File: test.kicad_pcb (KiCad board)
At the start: 2 copper layers, 110 x 100 mm, 203 parts, among them J1 HSP2_MX-502584-0670, J2 HSP2_MX-502584-0670, J3 HSP2_MX-502584-0670, J4 HSP2_MX-502584-0670, J5 HSP2_MX-502584-0670, J6 HSP2_MX-502584-0670, J7 CONN_02X01, J8 CONN_02X01, J9 microSD, P1 Gniazdo akumulatora, P2 Gniazdo akumulatora, P3 Gniazdo programatora SWD, T1 IRLML6401, T10 BSS138, T11 BSS138, T12 BSS138, T13 BSS138, T14 FDV304P, T2 IRLML6401, T3 IRLML6401, T4 IRLML6401, T5 IRLML6401, T6 IRLML6401, T7 BSS138, T8 BSS138, T9 BSS138, U1 MCP1755T-3302E/DC, U10 TPS3823, U11 STM32L051R8, U12 DS3231SN, U13 MCP1755T-3302E/DC, U14 MCP1755T-3302E/DC, U15 MIC29302, U16 DHT22, U17 M590E, U18 S25FL1275ABMGI101, U19 ESP-07, U2 MCP1755T-3302E/DC, U20 SIMHOLDER, U3 MCP1755T-3302E/DC, U4 MCP1755T-3302E/DC, U5 MCP1755T-3302E/DC, U6 MCP1755T-3302E/DC, U7 74LVX373M, U8 74LVX373M, U9 MAX3485, Y1 32.768 kHz, Y2 8 MHz

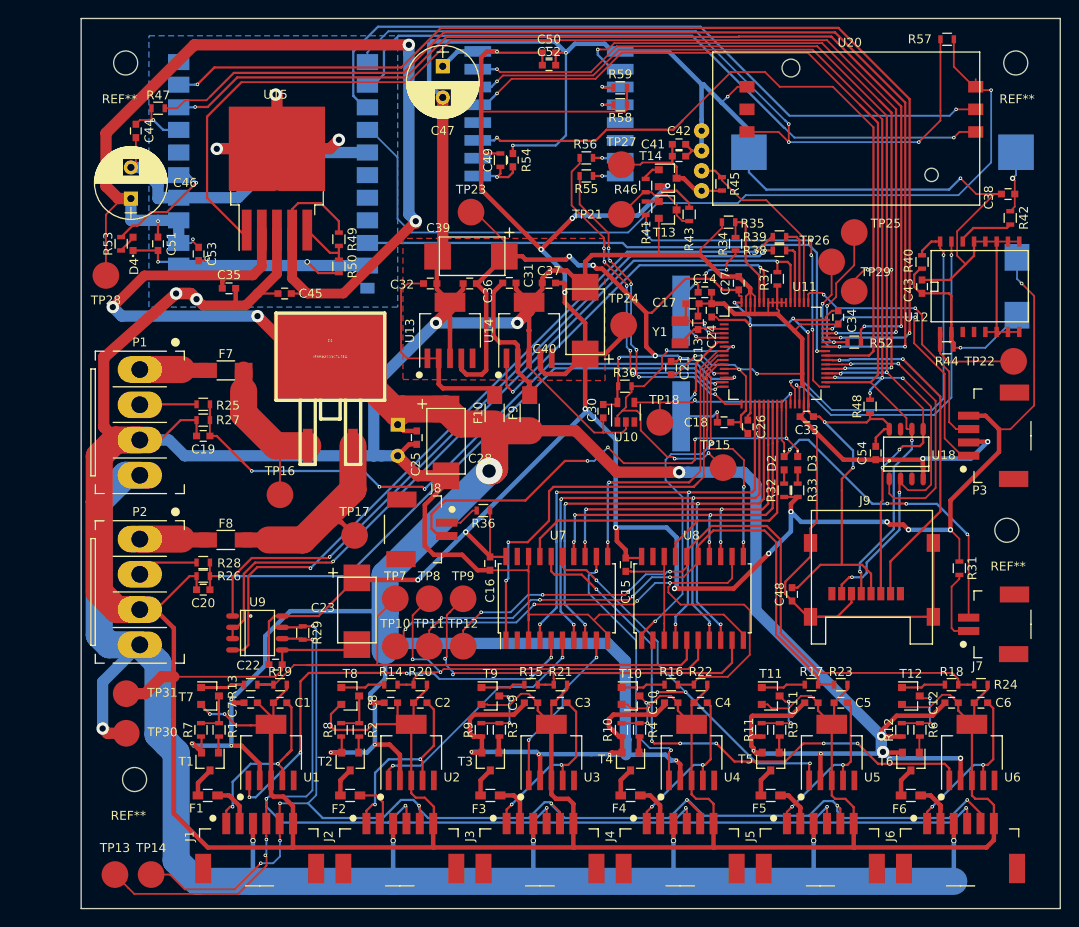
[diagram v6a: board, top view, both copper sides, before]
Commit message: +creo-weipu +zmiana dht22 i c1000
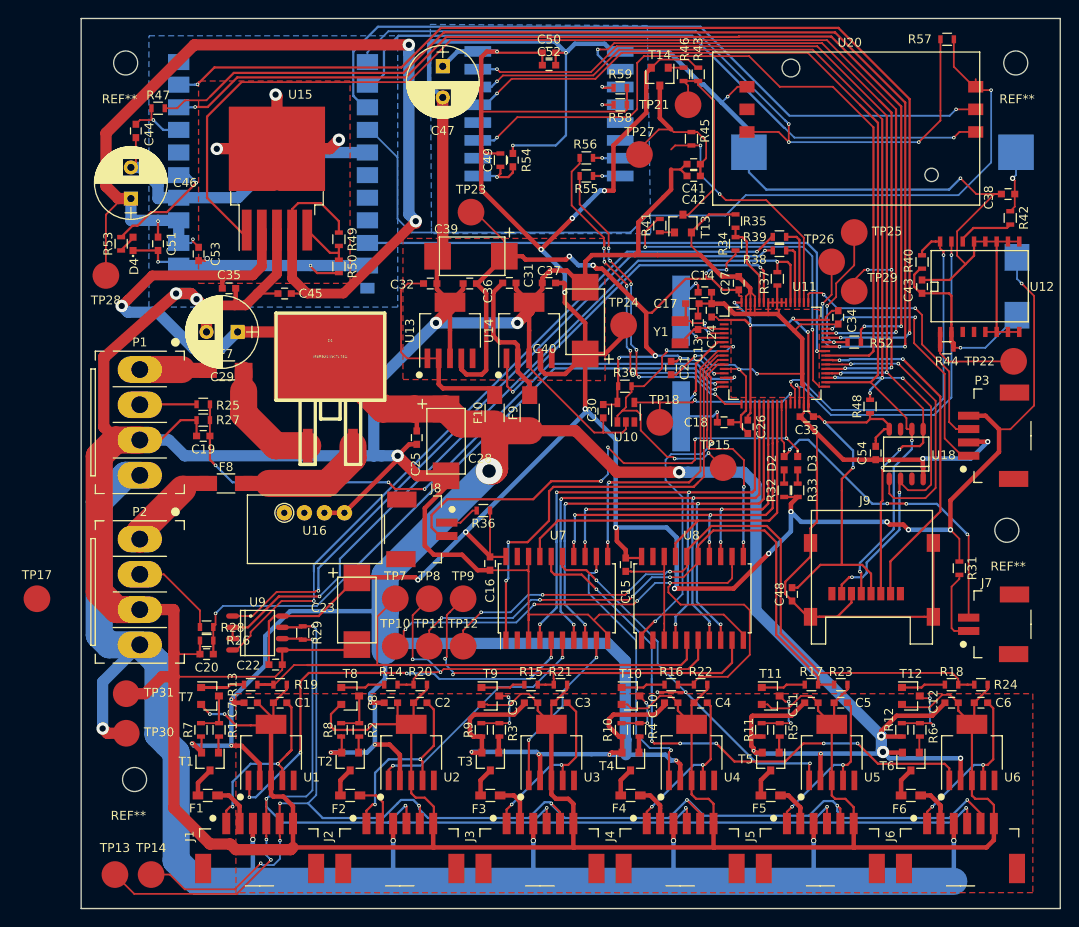
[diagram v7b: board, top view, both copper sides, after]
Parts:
- removed TP16: TEST, Measurement_Points:Measurement_Point_Round-SMD-Pad_Big
- C29, U16: moved to F.Cu
- moved U16 58.8 mm to (44.6, 129.5), turned to 180 degrees
- moved TP17 36.4 mm to (10.0, 139.2)
- moved C29 20.8 mm to (32.6, 109.2), turned to 180 degrees
- moved R43 15.8 mm to (84.3, 80.3)
- moved TP21 14.4 mm to (83.2, 83.7)
- moved R46 13.2 mm to (82.7, 80.3)
- moved T14 11.4 mm to (80.0, 80.5), turned to 270 degrees
- moved C20 7.25 mm to (29.1, 145.4)
- moved R26 7.25 mm to (29.1, 142.4)
- moved R28 7.25 mm to (29.1, 143.9)
- moved F8 6.35 mm to (31.3, 126.2)
- moved R45 6.12 mm to (83.6, 87.5), turned to 90 degrees
- moved C42 3.92 mm to (83.8, 91.7), turned to 180 degrees
- moved R41 2.52 mm to (80.0, 97.3), turned to 90 degrees
- moved TP27 2.33 mm to (77.7, 89.3)
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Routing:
- net GND: track 1085.5 -> 1103.8 mm, vias 21 -> 22
- net Net-(R43-Pad1): track 10.7 -> 22.1 mm
- net +3.3V: track 299.9 -> 309.5 mm
- net Net-(D1-Pad3): track 23.6 -> 14.8 mm
- net /DHT22_DATA: track 22.0 -> 28.6 mm, vias 0 -> 2
- net Net-(D1-Pad1): track 19.3 -> 14.2 mm
- net Net-(P2-Pad2): track 5.56 -> 10.3 mm
- net /ESP_ON: track 81.3 -> 85.5 mm
- net Net-(C41-Pad1): track 15.5 -> 19.4 mm
- net Net-(F8-Pad1): track 7.71 -> 11.0 mm
- net VBAT: track 396.6 -> 399.3 mm, vias 19 -> 18
- net /BAT2_POM: track 71.3 -> 74.0 mm
- net Net-(R34-Pad1): track 12.5 -> 9.97 mm
- net /485_DI: track 84.6 -> 82.5 mm
- net /485_RDE: track 89.7 -> 87.7 mm
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
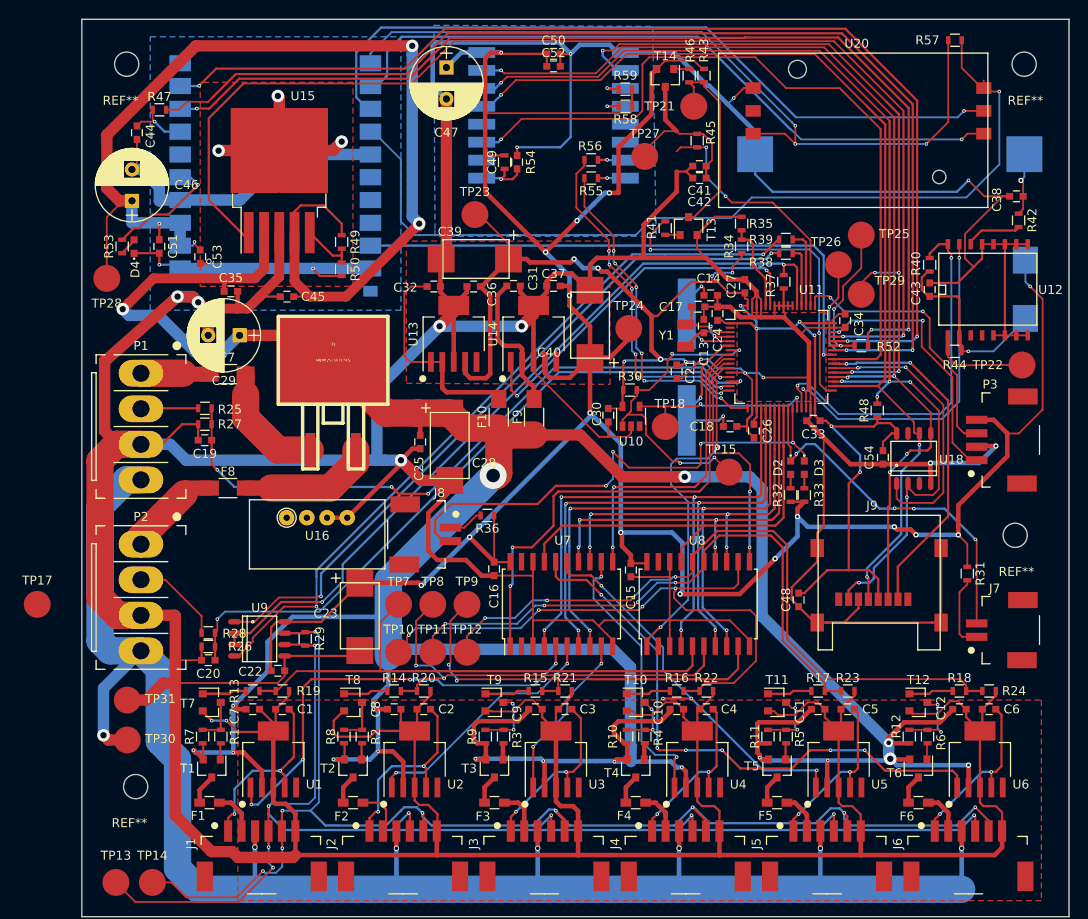
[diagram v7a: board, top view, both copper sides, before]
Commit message: +dht22 3d +mbr 3d -pliki posprzątane
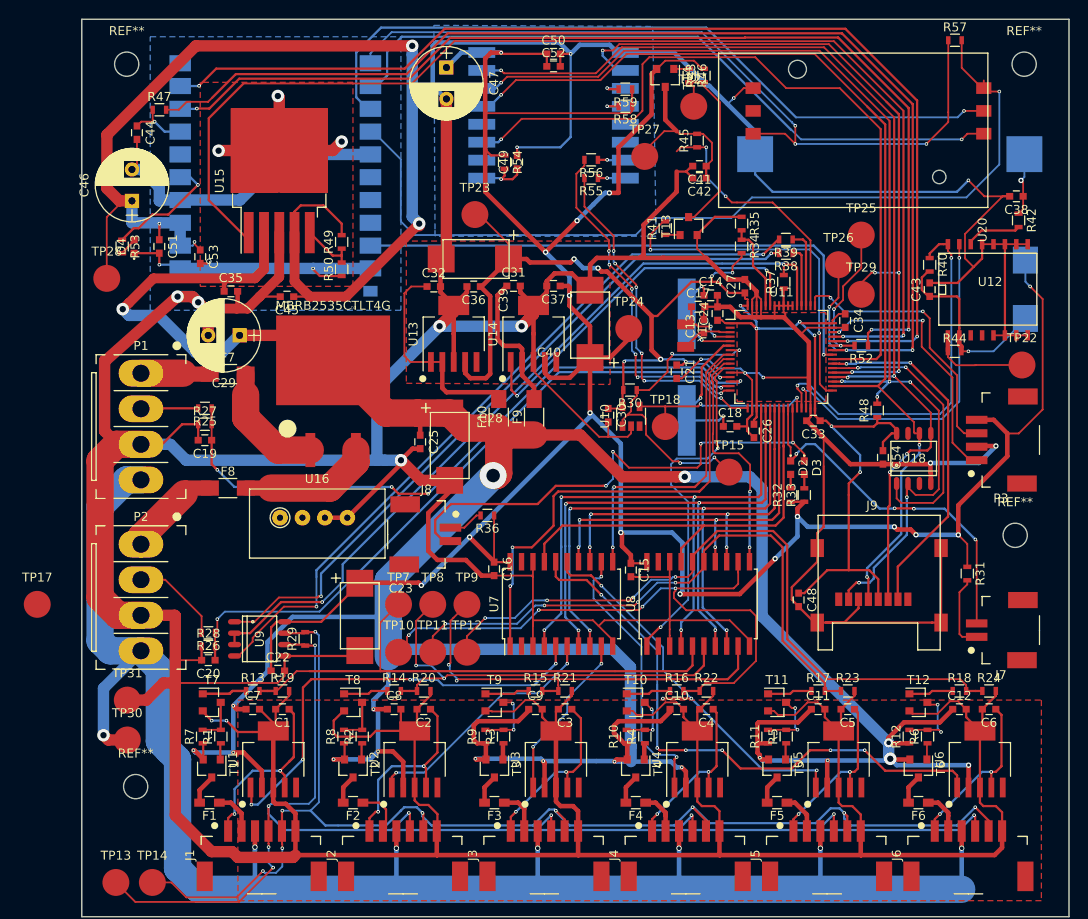
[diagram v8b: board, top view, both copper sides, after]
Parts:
- moved U16 4.92 mm to (40.8, 126.3)
